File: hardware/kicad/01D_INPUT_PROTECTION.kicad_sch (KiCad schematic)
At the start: 9 parts, among them Q401 IPD90N10S4-06 PROVISIONAL 100V, Q402 IPD90N10S4-06 PROVISIONAL 100V, U401 LM74930QRGERQ1_INCOMPLETE

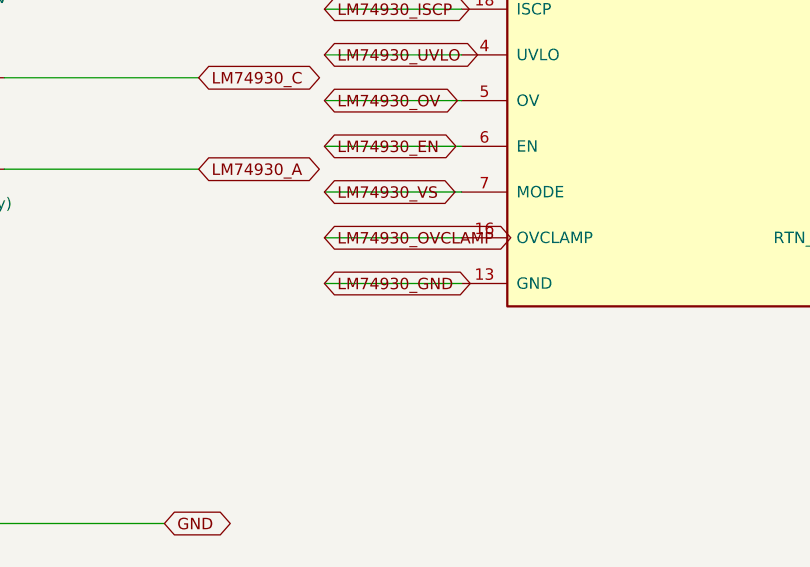
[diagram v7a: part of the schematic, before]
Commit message: fix(power): connect LM74930 GND pin 13 to actual global GND return
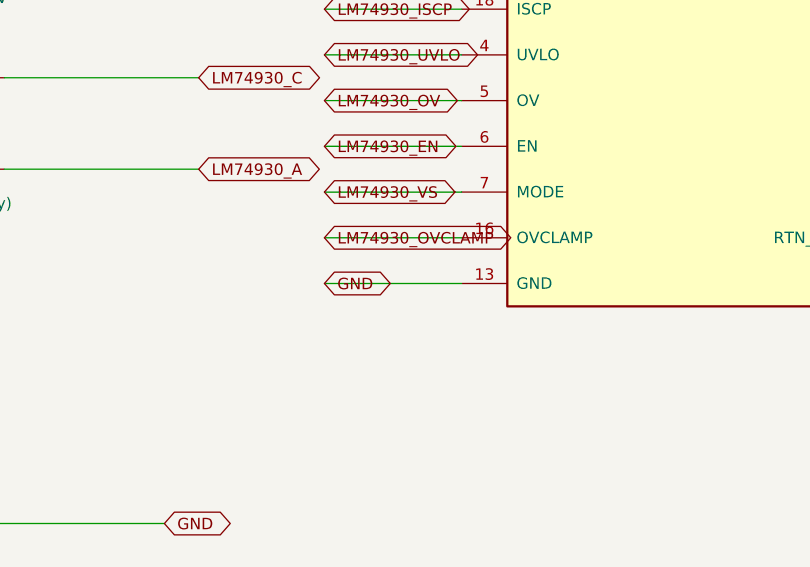
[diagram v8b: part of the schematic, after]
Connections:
- net LM74930_GND is gone; now on net GND: U401.13 (GND)
